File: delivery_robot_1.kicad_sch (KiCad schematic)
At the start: 46 parts, among them J1 SWD, J2 Conn_01x02, J3 UART, J4 BOOT0 jumper, SW1 RESET, U1 STM32F091RCTx, U2 PTPSM63606RDLR, U3 TPS54202DDCR, Y3 Crystal_GND24

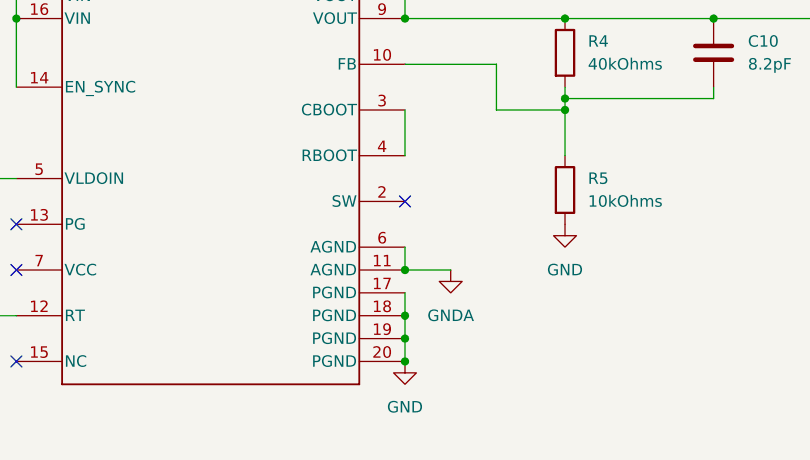
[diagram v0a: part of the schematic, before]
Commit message: Connect TPSM63606 analog ground to power ground per TI datasheet
Join U2's previously isolated AGND net to the system GND/PGND net.
AGND pins 6 and 11 now share the ground reference with PGND pins
17-20, the R2 frequency-setting resistor return, and the R5 feedback
divider return. This prevents the regulator's analog reference from
floating relative to its power stage and external setting resistors.

Reference: TI TPSM63606 datasheet, SLVSGB4B, Rev. B (April 2022),
Table 6-1, page 4: AGND must connect to PGND; RT and the lower feedback
resistor return to AGND. Section 11.1, page 31, specifies connecting
AGND pins 6 and 11 directly to PGND pin 19 under the module.
https://www.ti.com/lit/ds/symlink/tpsm63606.pdf

Validation: exported the saved schematic with KiCad 10.0.6 and compared
component-pin net assignments against the prior system netlist. Only
U2 pins 6 and 11 changed, from GNDA to GND; R2/R5 returns and all PGND
pins are on that same net. git diff --check passed.

ERC still reports 6 errors and 56 warnings, including a new multiple
net names warning because GND and GNDA symbols remain on the common
net. Other schematic review items are outside this change. The direct
under-module ground connection must still be implemented in PCB layout.
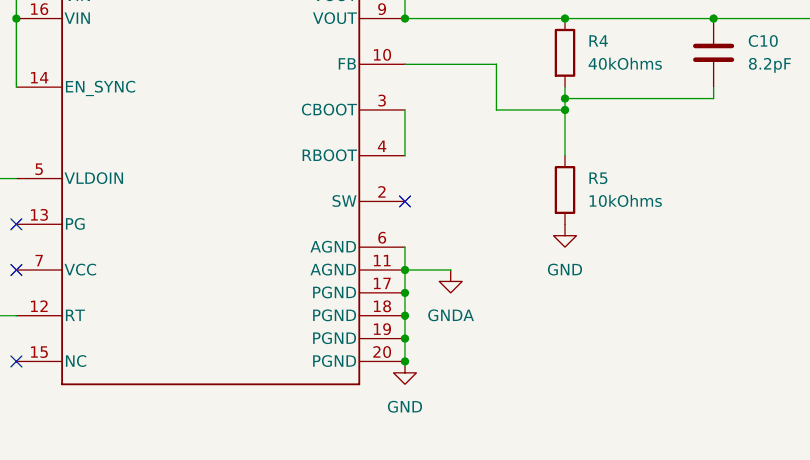
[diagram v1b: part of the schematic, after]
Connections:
- net GNDA is gone; now on net GND: U2.11 (AGND), U2.6 (AGND)
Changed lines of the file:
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@@
+	)
+	(junction
+		(at 86.36 264.16)
+		(diameter 0)
+		(color 0 0 0 0)
 	)
 	(junction
@@
 		)
 		(stroke
+			(width 0)
+			(type default)
+		)
+	)
+	(wire
+		(pts
+			(xy 86.36 261.62) (xy 86.36 264.16)
+		)
+		(stroke

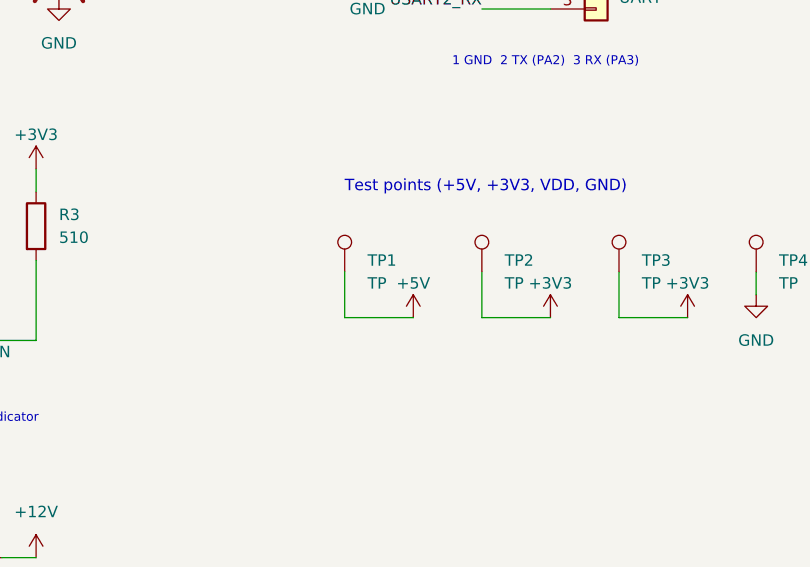
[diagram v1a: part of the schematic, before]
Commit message: Connect TP1 to the 5 V, 2 A buck output net
Rename the power symbol attached to TP1 from +5V to +5V, 2A so the
connection point belongs to the TPS54202 output after L1. Previously,
+5V was a separate net containing only TP1 and did not connect to
either buck output. This makes TP1 usable for accessing the intended
2 A supply and keeps the 6 A supply electrically separate.

Validation: exported the saved schematic using KiCad 10.0.6 and
compared component-pin net assignments with the preceding revision.
Only TP1 pin 1 changed nets. It now shares +5V, 2A with L1 pin 1,
C17, the feedback divider upper connection, and the LDO input/enable.
The +5V, 6A net is unchanged. git diff --check passed.

TP1 retains its existing TestPoint_Pad_D1.5mm footprint; this change
does not add a header footprint or the future off-board Pi connection.
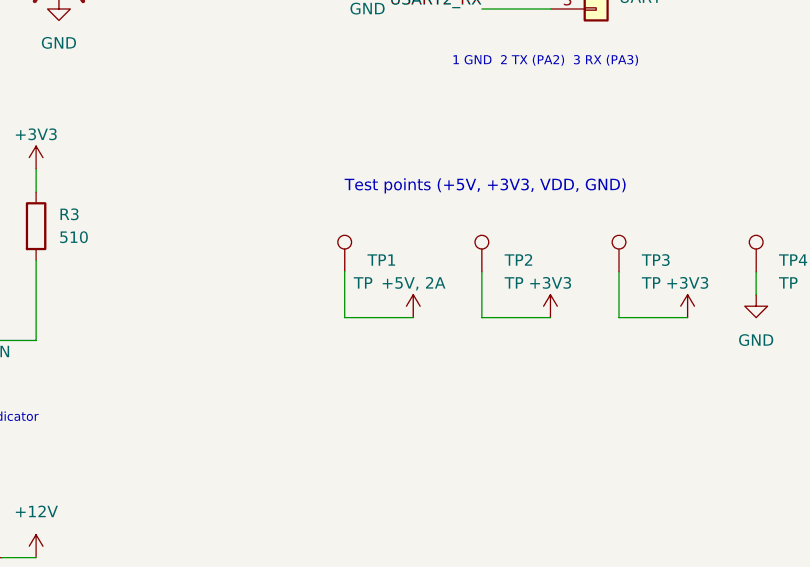
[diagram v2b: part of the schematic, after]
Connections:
- net +5V is gone; now on net +5V, 2A: TP1.1
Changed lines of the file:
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@@
 		)
 		(property "Value" "TP"
-			(at 85.09 137.16 0)
+			(at 83.566 137.16 0)
 			(show_name no)
 			(do_not_autoplace no)
@@
 			)
 		)
-		(property "Value" "+5V"
+		(property "Value" "+5V, 2A"
 			(at 90.17 137.16 0)
 			(show_name no)

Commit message: Standardize every resistor footprint to the required 0805 package
Assign Resistor_SMD:R_0805_2012Metric to all system resistors R1-R9
and both resistors in the reusable LDO schematic. This meets the
team's requirement that every resistor use 0805, fills the five
missing system resistor footprints, and replaces existing 0603
assignments. Document the requirement and remaining part-rating checks.

Validation: the installed KiCad 0805 footprint exists. Exported
before/after system netlists confirm all nine resistor footprints are
0805 and every component value and electrical net connection is
unchanged. Resistance tolerances are preserved. git diff --check passed.

Purchasing parts must still match the specified resistance/tolerance
and provide suitable power and working-voltage ratings.
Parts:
- R1, R3: footprint Resistor_SMD:R_0603_1608Metric -> Resistor_SMD:R_0805_2012Metric
- R2, R4, R5, R6, R7: footprint (none) -> Resistor_SMD:R_0805_2012Metric
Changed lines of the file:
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@@
 			)
 		)
-		(property "Footprint" ""
+		(property "Footprint" "Resistor_SMD:R_0805_2012Metric"
 			(at 102.362 186.69 90)
 			(hide yes)
@@
 			)
 		)
-		(property "Footprint" "Resistor_SMD:R_0603_1608Metric"
+		(property "Footprint" "Resistor_SMD:R_0805_2012Metric"
 			(at 72.39 66.04 0)
 			(hide yes)
@@
 			)
 		)
-		(property "Footprint" ""
+		(property "Footprint" "Resistor_SMD:R_0805_2012Metric"
 			(at 102.362 252.73 90)
 			(hide yes)
@@
 			)
 		)
-		(property "Footprint" "Resistor_SMD:R_0603_1608Metric"
+		(property "Footprint" "Resistor_SMD:R_0805_2012Metric"
 			(at 48.26 130.81 0)
 			(hide yes)
@@
 			)
 		)
-		(property "Footprint" ""
+		(property "Footprint" "Resistor_SMD:R_0805_2012Metric"
 			(at 102.362 237.49 90)
 			(hide yes)
@@
 			)
 		)
-		(property "Footprint" ""
+		(property "Footprint" "Resistor_SMD:R_0805_2012Metric"
 			(at 31.242 270.51 90)
 			(hide yes)
@@
 			)
 		)
-		(property "Footprint" ""
+		(property "Footprint" "Resistor_SMD:R_0805_2012Metric"
 			(at 102.362 199.39 90)
 			(hide yes)

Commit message: Select datasheet-backed power capacitors and inductor footprints
Assign the ten missing buck capacitor footprints and L1, with actual
manufacturer part numbers, ratings and source links. Select 1210
Murata capacitors for the TPSM63606 input/output banks, 0603 ceramics
for bypass/bootstrap/feedforward roles, and a 50 V TDK 2220 part for
the existing 22 uF TPS54202 input capacitor. Keep all capacitances.
Complete LDO noise/bypass capacitor part numbers and replace the input
capacitor ordering number with a matching 1 uF 16 V 0603 Murata part;
keep the reusable LDO example consistent.

Change L1 from 10 uH to 15 uH and select Coilcraft XAL6060-153MEC.
At 2 A output, 28 V input, 390 kHz and -20% inductance tolerance,
estimated peak current is 2.439 A rather than 2.658 A for 10 uH.
The selected part has 5.8 A typical saturation current, 4.5 A thermal
reference current at 20 C rise, and 43.75 milliohm maximum DCR.
Its installed footprint matches Coilcraft's 1.43 x 5.50 mm pads on
4.04 mm centers. Normal battery range supplied by the user is
10.8-14.6 V; no bounded motor-transient voltage is assumed.

References:
TI TPSM63606 SLVSGB4B Rev. B, Tables 8-1/8-2/8-3, pp. 16-17,
and section 9.2.1.2.5, p. 24:
https://www.ti.com/lit/ds/symlink/tpsm63606.pdf
TI TPS54202 SLVSD26C Rev. C, section 7.2.3.5 and Table 7-2, pp. 15-17:
https://www.ti.com/lit/gpn/tps54202
Coilcraft XAL60xx Document 887 (02/25/26), pp. 1 and 4:
https://www.coilcraft.com/getmedia/ea51f14b-7f32-4dc6-8dfe-d4b70549040f/xal60xx.pdf
TDK C14 specifications and recommended land-pattern ranges:
https://product.tdk.com/en/search/capacitor/ceramic/mlcc/info?part_no=C5750X7R1H226M250KB

Provide a project-local C14 footprint using TDK's land-pattern ranges
(4.2 mm inner gap, 1.3 mm pad width, 5.0 mm pad height) instead of
assuming the generic 2220 footprint matches. Document all purchasing
candidates and sources in docs/passive-selection-review.md and JSON.

Validation: KiCad export succeeds; before/after component-pin n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
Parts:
- C10: footprint (none) -> Capacitor_SMD:C_0603_1608Metric; MPN (none) -> GRM1885C1H8R2DA01D; Manufacturer (none) -> Murata; Specification (none) -> 8.2pF / 50V C0G
- C11, C12, C17: footprint (none) -> project_footprints:C_Murata_GRM32ER71A476ME15; MPN (none) -> GRM32ER71A476ME15L; Manufacturer (none) -> Murata; Specification (none) -> 47uF / 10V X7R
- C14: footprint (none) -> project_footprints:C_TDK_C5750X7R1H226M250KB; MPN (none) -> C5750X7R1H226M250KB; Manufacturer (none) -> TDK; Specification (none) -> 22uF / 50V X7R
- C15: footprint (none) -> Capacitor_SMD:C_0603_1608Metric; MPN (none) -> C1608X7R1H104K080AA; Manufacturer (none) -> TDK; Specification (none) -> 100nF / 50V X7R
- C16: footprint (none) -> Capacitor_SMD:C_0603_1608Metric; MPN (none) -> GRM1885C1H680JA01D; Manufacturer (none) -> Murata; Specification (none) -> 68pF / 50V C0G
- C7, C8: footprint (none) -> Capacitor_SMD:C_1210_3225Metric; MPN (none) -> GRM32ER71H106KA12L; Manufacturer (none) -> Murata; Specification (none) -> 10uF / 50V X7R
- C9: footprint (none) -> Capacitor_SMD:C_0603_1608Metric; MPN (none) -> GRM188R71C105KA12D; Manufacturer (none) -> Murata; Specification (none) -> 1uF / 16V X7R
- L1: value 10uH -> 15uH; footprint (none) -> Inductor_SMD:L_Coilcraft_XAL6060-XXX; MPN (none) -> XAL6060-153MEC; Manufacturer (none) -> Coilcraft; Specification (none) -> 15uH / 20%
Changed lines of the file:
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@@
 			)
 		)
-		(property "Footprint" ""
+		(property "Footprint" "Capacitor_SMD:C_0603_1608Metric"
 			(at 93.6752 190.5 0)
 			(hide yes)
@@
 			)
 		)
-		(property "Datasheet" ""
+		(property "Datasheet" "https://search.murata.co.jp/Ceramy/image/img/A01X/G101/ENG/GRM1885C1H680JA01-01A.pdf"
 			(at 92.71 186.69 0)
 			(hide yes)
@@
 			)
 		)
+		(property "Manufacturer" "Murata"
+			(at 92.71 186.69 0)
+			(hide yes)
+			(effects (font (size 1.27 1.27)))
+		)
+		(property "MPN" "GRM1885C1H680JA01D"
+			(at 92.71 186.69 0)
+			(hide yes)
+			(effects (font (size 1.27 1.27)))
+		)
+		(property "Specification" "68pF / 50V C0G"
+			(at 0 0 0)
+			(hide yes)
+			(effects (font (size 1.27 1.27)))
+		)
 	)
 	(symbol
@@
 			)
 		)
-		(property "Footprint" ""
+		(property "Footprint" "project_footprints:C_TDK_C5750X7R1H226M250KB"
 			(at 18.7452 194.31 0)
 			(hide yes)
@@
 			)
 		)
-		(property "Datasheet" ""
+		(property "Datasheet" "https://product.tdk.com/en/search/capacitor/ceramic/mlcc/info?part_no=C5750X7R1H226M250KB"
 			(at 17.78 190.5 0)
 			(hide yes)
@@
 			)
 		)
+		(property "Manufacturer" "TDK"
+			(at 17.78 190.5 0)
+			(hide yes)
+			(effects (font (size 1.27 1.27)))
+		)
+		(property "MPN" "C5750X7R1H226M250KB"
+			(at 17.78 190.5 0)
+			(hide yes)
+			(effects (font (size 1.27 1.27)))
+		)
+		(property "Specification" "22uF / 50V X7R"
+			(at 0 0 0)
+			(hide yes)
+			(effects (font (size 1.27 1.27)))
+		)
 	)
 	(symbol
@@
 			)
 		)
-		(property "Footprint" ""
+		(property "Footprint" "project_footprints:C_Murata_GRM32ER71A476ME15"
 			(at 148.2852 241.3 0)
 			(hide yes)
@@
 			)
 		)
-		(property "Datasheet" ""
+		(property "Datasheet" "https://search.murata.co.jp/Ceramy/image/img/A01X/G101/ENG/GRM32ER71A476ME15-04CA.pdf"
 			(at 147.32 237.49 0)
 			(hide yes)
@@
 			)
 		)
+		(property "Manufacturer" "Murata"
+			(at 147.32 237.49 0)
+			(hide yes)
+			(effects (font (size 1.27 1.27)))
+		)
+		(property "MPN" "GRM32ER71A476ME15L"
+			(at 147.32 237.49 0)
+			(hide yes)
+			(effects (font (size 1.27 1.27)))
+		)
+		(property "Specification" "47uF / 10V X7R"
+			(at 0 0 0)
+			(hide yes)
+			(effects (font (size 1.27 1.27)))
+		)
 	)
 	(symbol
@@
 			)
 		)
-		(property "Footprint" ""
+		(property "Footprint" "project_footprints:C_Murata_GRM32ER71A476ME15"
 			(at 124.1552 196.85 0)
 			(hide yes)
@@
 			)
 		)
-		(property "Datasheet" ""
+		(property "Datasheet" "https://search.murata.co.jp/Ceramy/image/img/A01X/G101/ENG/GRM32ER71A476ME15-04CA.pdf"
 			(at 123.19 193.04 0)
 			(hide yes)
@@
 			)
 		)
+		(property "Manufacturer" "Murata"
+			(at 123.19 193.04 0)
+			(hide yes)
+			(effects (font (size 1.27 1.27)))
+		)
+		(property "MPN" "GRM32ER71A476ME15L"
+			(at 123.19 193.04 0)
+			(hide yes)
+			(effects (font (size 1.27 1.27)))
+		)
+		(property "Specification" "47uF / 10V X7R"
+			(at 0 0 0)
+			(hide yes)
+			(effects (font (size 1.27 1.27)))
+		)
 	)
 	(symbol
@@
 			)
 		)
-		(property "Footprint" ""
+		(property "Footprint" "Capacitor_SMD:C_0603_1608Metric"
 			(at 121.6152 241.3 0)
 			(hide yes)
@@
 			)
 		)
-		(property "Datasheet" ""
+		(property "Datasheet" "https://search.murata.co.jp/Ceramy/image/img/A01X/G101/ENG/GRM1885C1H8R2DA01-01A.pdf"
 			(at 120.65 237.49 0)
 			(hide yes)
@@
 			)
 		)
+		(property "Manufacturer" "Murata"
+			(at 120.65 237.49 0)
+			(hide yes)
+			(effects (font (size 1.27 1.27)))
+		)
+		(property "MPN" "GRM1885C1H8R2DA01D"
+			(at 120.65 237.49 0)
+			(hide yes)
+			(effects (font (size 1.27 1.27)))
+		)
+		(property "Specification" "8.2pF / 50V C0G"
+			(at 0 0 0)
+			(hide yes)
+			(effects (font (size 1.27 1.27)))
+		)
 	)
 	(symbol
@@
 			)
 		)
-		(property "Footprint" ""
+		(property "Footprint" "Capacitor_SMD:C_0603_1608Metric"
 			(at 78.74 181.9148 0)
 			(hide yes)
@@
 			)
 		)
-		(property "Datasheet" ""
+		(property "Datasheet" "https://product.tdk.com/en/search/capacitor/ceramic/mlcc/info?part_no=C1608X7R1H104K080AA"
 			(at 74.93 182.88 0)
 			(hide yes)
@@
 			)
 		)
+		(property "Manufacturer" "TDK"
+			(at 74.93 182.88 0)
+			(hide yes)
+			(effects (font (size 1.27 1.27)))
+		)
+		(property "MPN" "C1608X7R1H104K080AA"
+			(at 74.93 182.88 0)
+			(hide yes)
+			(effects (font (size 1.27 1.27)))
+		)
+		(property "Specification" "100nF / 50V X7R"
+			(at 0 0 0)
+			(hide yes)
+			(effects (font (size 1.27 1.27)))
+		)
 	)
 	(symbol
@@
 			)
 		)
-		(property "Footprint" ""
+		(property "Footprint" "Capacitor_SMD:C_0603_1608Metric"
 			(at 31.4452 259.08 0)
 			(hide yes)
@@
 			)
 		)
-		(property "Datasheet" ""
+		(property "Datasheet" "https://search.murata.co.jp/Ceramy/image/img/A01X/G101/ENG/GRM188R71C105KA12-01.pdf"
 			(at 30.48 255.27 0)
 			(hide yes)
@@
 			)
 		)
+		(property "Manufacturer" "Murata"
+			(at 30.48 255.27 0)
+			(hide yes)
+			(effects (font (size 1.27 1.27)))
+		)
+		(property "MPN" "GRM188R71C105KA12D"
+			(at 30.48 255.27 0)
+			(hide yes)
+			(effects (font (size 1.27 1.27)))
+		)
+		(property "Specification" "1uF / 16V X7R"
+			(at 0 0 0)
+			(hide yes)
+			(effects (font (size 1.27 1.27)))
+		)
 	)
 	(symbol
@@
 			)
 		)
-		(property "Footprint" ""
+		(property "Footprint" "Capacitor_SMD:C_1210_3225Metric"
 			(at 18.7452 236.22 0)
 			(hide yes)
@@
 			)
 		)
-		(property "Datasheet" ""
+		(property "Datasheet" "https://search.murata.co.jp/Ceramy/image/img/A01X/G101/ENG/GRM32ER71H106KA12-04A.pdf"
 			(at 17.78 232.41 0)
 			(hide yes)
@@
 			)
 		)
+		(property "Manufacturer" "Murata"
+			(at 17.78 232.41 0)
+			(hide yes)
+			(effects (font (size 1.27 1.27)))
+		)
+		(property "MPN" "GRM32ER71H106KA12L"
+			(at 17.78 232.41 0)
+			(hide yes)
+			(effects (font (size 1.27 1.27)))
+		)
+		(property "Specification" "10uF / 50V X7R"
+			(at 0 0 0)
+			(hide yes)
+			(effects (font (size 1.27 1.27)))
+		)
 	)
 	(symbol
@@
 			)
 		)
-		(property "Footprint" ""
+		(property "Footprint" "project_footprints:C_Murata_GRM32ER71A476ME15"
 			(at 135.5852 241.3 0)
 			(hide yes)
@@
 			)
 		)
-		(property "Datasheet" ""
+		(property "Datasheet" "https://search.murata.co.jp/Ceramy/image/img/A01X/G101/ENG/GRM32ER71A476ME15-04CA.pdf"
 			(at 134.62 237.49 0)
 			(hide yes)
@@
 			)
 		)
+		(property "Manufacturer" "Murata"
+			(at 134.62 237.49 0)
+			(hide yes)
+			(effects (font (size 1.27 1.27)))
+		)
+		(property "MPN" "GRM32ER71A476ME15L"
+			(at 134.62 237.49 0)
+			(hide yes)
+			(effects (font (size 1.27 1.27)))
+		)
+		(property "Specification" "47uF / 10V X7R"
+			(at 0 0 0)
+			(hide yes)
+			(effects (font (size 1.27 1.27)))
+		)
 	)
 	(symbol
@@
 			)
 		)
-		(property "Value" "10uH"
+		(property "Value" "15uH"
 			(at 85.09 180.34 90)
 			(show_name no)
@@
 			)
 		)
-		(property "Footprint" ""
+		(property "Footprint" "Inductor_SMD:L_Coilcraft_XAL6060-XXX"
 			(at 85.09 182.88 0)
 			(hide yes)
@@
 			)
 		)
-		(property "Datasheet" ""
+		(property "Datasheet" "https://www.coilcraft.com/getmedia/ea51f14b-7f32-4dc6-8dfe-d4b70549040f/xal60xx.pdf"
 			(at 85.09 182.88 0)
 			(hide yes)
@@
 			)
 		)
+		(property "Manufacturer" "Coilcraft"
+			(at 85.09 182.88 0)
+			(hide yes)
+			(effects (font (size 1.27 1.27)))
+		)
+		(property "MPN" "XAL6060-153MEC"
+			(at 85.09 182.88 0)
+			(hide yes)
+			(effects (font (size 1.27 1.27)))
+		)
+		(property "Specification" "15uH / 20%"
+			(at 0 0 0)
+			(hide yes)
+			(effects (font (size 1.27 1.27)))
+		)
 	)
 	(symbol
@@
 			)
 		)
-		(property "Footprint" ""
+		(property "Footprint" "Capacitor_SMD:C_1210_3225Metric"
 			(at 31.4452 236.22 0)
 			(hide yes)
@@
 			)
 		)
-		(property "Datasheet" ""
+		(property "Datasheet" "https://search.murata.co.jp/Ceramy/image/img/A01X/G101/ENG/GRM32ER71H106KA12-04A.pdf"
 			(at 30.48 232.41 0)
 			(hide yes)
@@
 			)
 		)
+		(property "Manufacturer" "Murata"
+			(at 30.48 232.41 0)
+			(hide yes)
+			(effects (font (size 1.27 1.27)))
+		)
+		(property "MPN" "GRM32ER71H106KA12L"
+			(at 30.48 232.41 0)
+			(hide yes)
+			(effects (font (size 1.27 1.27)))
+		)
+		(property "Specification" "10uF / 50V X7R"
+			(at 0 0 0)
+			(hide yes)
+			(effects (font (size 1.27 1.27)))
+		)
 	)
